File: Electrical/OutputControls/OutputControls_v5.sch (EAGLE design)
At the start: 13 parts, among them IC1 MCP23008

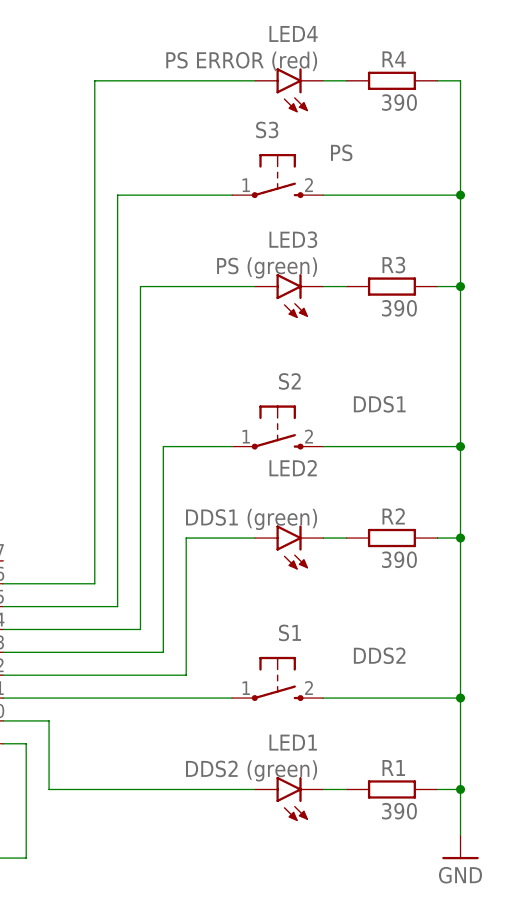
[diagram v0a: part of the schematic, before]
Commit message: Updated OutputControls and MainBoard in Electrical folder
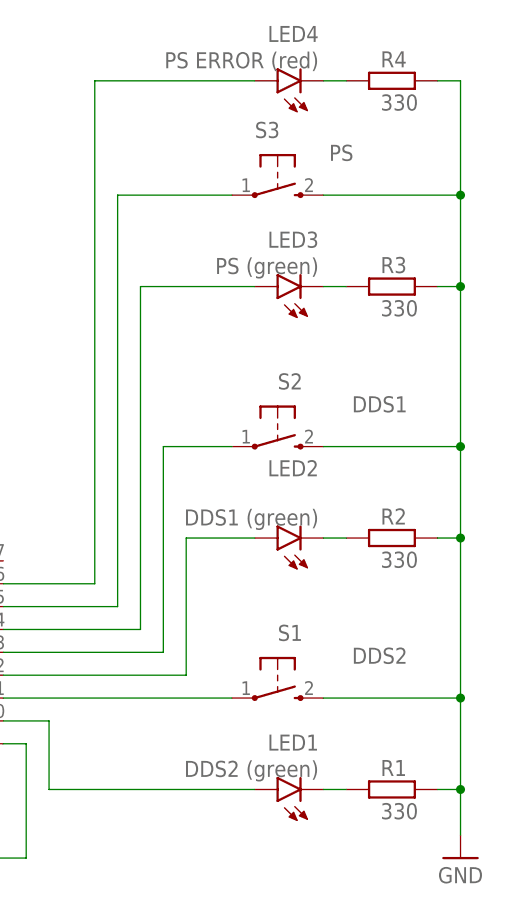
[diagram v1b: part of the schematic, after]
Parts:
- R1, R2, R3, R4: value 390 -> 330
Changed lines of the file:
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@@
 <layer number="155" name="FabDoc3" color="7" fill="1" visible="yes" active="yes"/>
 <layer number="199" name="Contour" color="7" fill="1" visible="yes" active="yes"/>
-<layer number="200" name="200bmp" color="7" fill="1" visible="no" active="yes"/>
+<layer number="200" name="200bmp" color="7" fill="10" visible="no" active="yes"/>
 <layer number="201" name="201bmp" color="7" fill="10" visible="yes" active="yes"/>
 <layer number="202" name="202bmp" color="7" fill="10" visible="yes" active="yes"/>
@@
 <part name="LED2" library="OwnDevices" library_urn="urn:adsk.wipprod:fs.file:vf.a4uZ8vxKQaeHmtfASYy_rA" deviceset="LED" device="CHIPLED_0603" package3d_urn="urn:adsk.eagle:package:15822/2" value="DDS1 (green)"/>
 <part name="LED3" library="OwnDevices" library_urn="urn:adsk.wipprod:fs.file:vf.a4uZ8vxKQaeHmtfASYy_rA" deviceset="LED" device="CHIPLED_0603" package3d_urn="urn:adsk.eagle:package:15822/2" value="PS (green)"/>
-<part name="R1" library="OwnDevices" library_urn="urn:adsk.wipprod:fs.file:vf.a4uZ8vxKQaeHmtfASYy_rA" deviceset="R-EU_" device="R0805" package3d_urn="urn:adsk.eagle:package:23553/2" value="390"/>
-<part name="R2" library="OwnDevices" library_urn="urn:adsk.wipprod:fs.file:vf.a4uZ8vxKQaeHmtfASYy_rA" deviceset="R-EU_" device="R0805" package3d_urn="urn:adsk.eagle:package:23553/2" value="390"/>
-<part name="R3" library="OwnDevices" library_urn="urn:adsk.wipprod:fs.file:vf.a4uZ8vxKQaeHmtfASYy_rA" deviceset="R-EU_" device="R0805" package3d_urn="urn:adsk.eagle:package:23553/2" value="390"/>
+<part name="R1" library="OwnDevices" library_urn="urn:adsk.wipprod:fs.file:vf.a4uZ8vxKQaeHmtfASYy_rA" deviceset="R-EU_" device="R0805" package3d_urn="urn:adsk.eagle:package:23553/2" value="330"/>
+<part name="R2" library="OwnDevices" library_urn="urn:adsk.wipprod:fs.file:vf.a4uZ8vxKQaeHmtfASYy_rA" deviceset="R-EU_" device="R0805" package3d_urn="urn:adsk.eagle:package:23553/2" value="330"/>
+<part name="R3" library="OwnDevices" library_urn="urn:adsk.wipprod:fs.file:vf.a4uZ8vxKQaeHmtfASYy_rA" deviceset="R-EU_" device="R0805" package3d_urn="urn:adsk.eagle:package:23553/2" value="330"/>
 <part name="SUPPLY1" library="Power_Symbols" library_urn="urn:adsk.eagle:library:16502351" deviceset="GND-BAR" device="" value="GND"/>
 <part name="SUPPLY2" library="Power_Symbols" library_urn="urn:adsk.eagle:library:16502351" deviceset="GND-BAR" device="" value="GND"/>
@@
 <part name="SUPPLY4" library="Power_Symbols" library_urn="urn:adsk.eagle:library:16502351" deviceset="+5V" device="" value="+5V"/>
 <part name="LED4" library="OwnDevices" library_urn="urn:adsk.wipprod:fs.file:vf.a4uZ8vxKQaeHmtfASYy_rA" deviceset="LED" device="CHIPLED_0603" package3d_urn="urn:adsk.eagle:package:15822/2" value="PS ERROR (red)"/>
-<part name="R4" library="OwnDevices" library_urn="urn:adsk.wipprod:fs.file:vf.a4uZ8vxKQaeHmtfASYy_rA" deviceset="R-EU_" device="R0805" package3d_urn="urn:adsk.eagle:package:23553/2" value="390"/>
+<part name="R4" library="OwnDevices" library_urn="urn:adsk.wipprod:fs.file:vf.a4uZ8vxKQaeHmtfASYy_rA" deviceset="R-EU_" device="R0805" package3d_urn="urn:adsk.eagle:package:23553/2" value="330"/>
 </parts>
 <sheets>
